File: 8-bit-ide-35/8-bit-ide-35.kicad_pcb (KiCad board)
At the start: 2 copper layers, 214 x 100.3 mm, 21 parts, among them U4 RPI_PICO

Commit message: Small schematic changes. Add outline of XTA board.
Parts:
- moved C1 84.4 mm to (75.1, 32.3)
- moved D1 84.4 mm to (46.7, 32.3)
- moved D2 84.4 mm to (52.4, 32.3)
- moved R10 84.4 mm to (69.0, 35.6)
- moved R11 84.4 mm to (69.0, 38.9)
- moved R12 84.4 mm to (46.6, 42.2)
- moved R14 84.4 mm to (57.8, 42.2)
- moved R2 84.4 mm to (57.8, 38.9)
- moved R4 84.4 mm to (46.6, 38.9)
- moved R7 84.4 mm to (57.8, 35.6)
- moved R9 84.4 mm to (46.6, 35.6)
- moved C3 84.4 mm to (63.8, 32.3)
- moved C4 84.4 mm to (69.4, 32.3)
- moved R1 84.4 mm to (63.4, 38.9)
- moved R3 84.4 mm to (52.2, 38.9)
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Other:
- board size 214 x 100.3 mm -> 222.1 x 98.7 mm

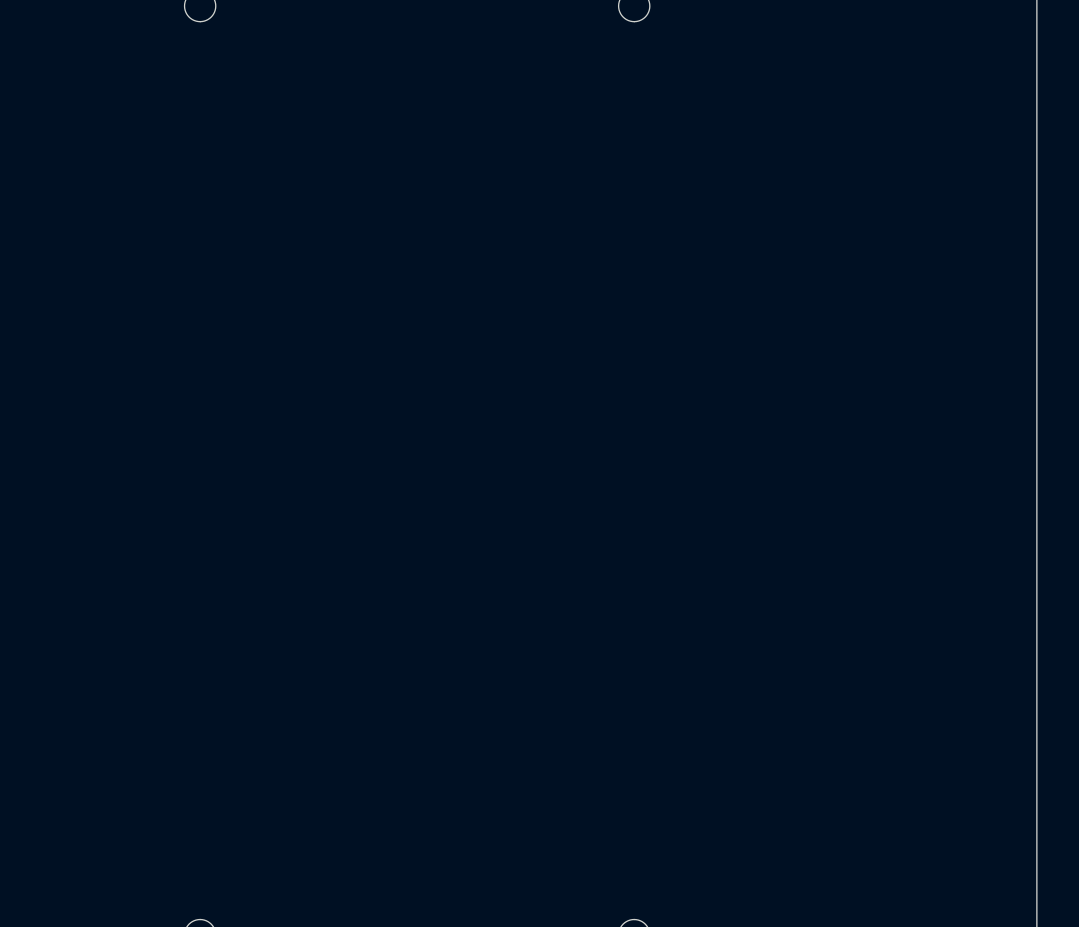
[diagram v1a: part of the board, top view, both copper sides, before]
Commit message: Add power and IDE cable connector. Add holes for mounting to 2.5" to 3.5" HDD adapter.
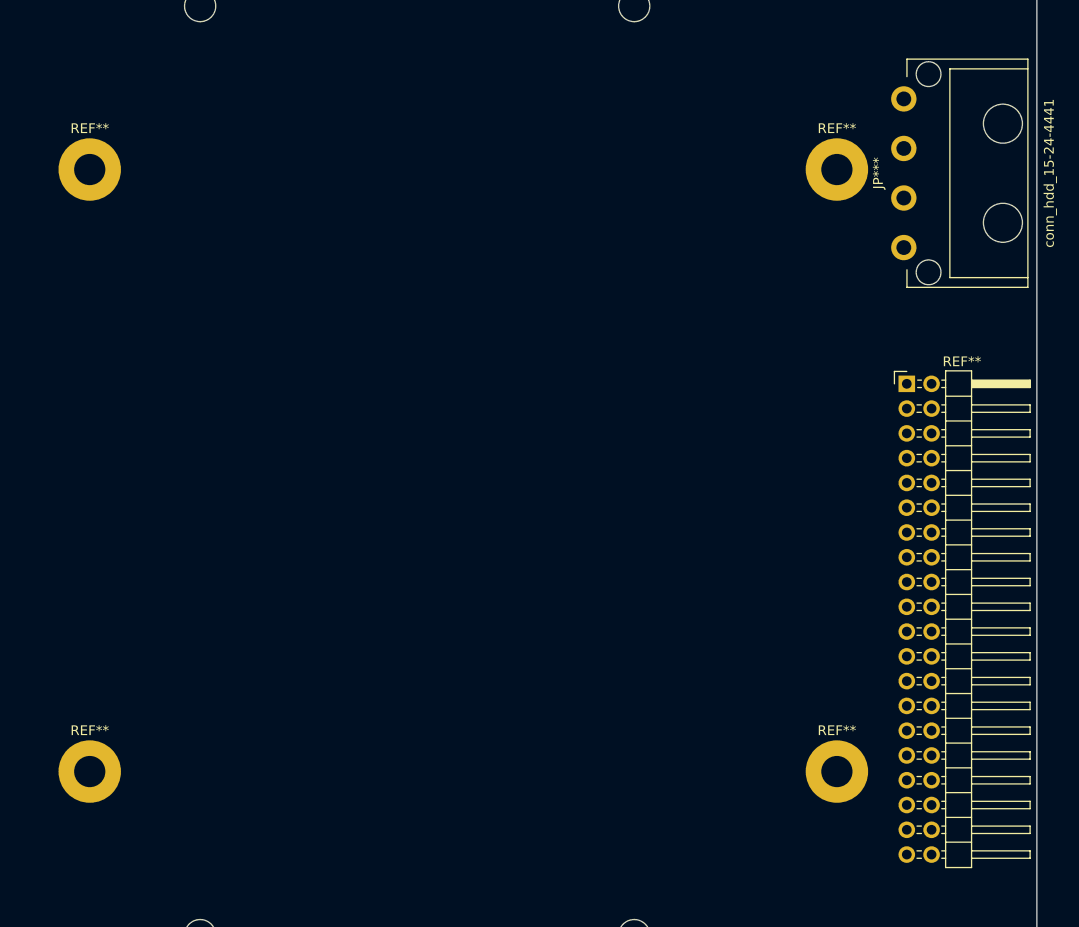
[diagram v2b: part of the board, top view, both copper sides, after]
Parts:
- added REF**: MountingHole_3.2mm_M3_Pad, MountingHole:MountingHole_3.2mm_M3_Pad, F.Cu at (153.1, 49.1)
- added REF**: MountingHole_3.2mm_M3_Pad, MountingHole:MountingHole_3.2mm_M3_Pad, F.Cu at (153.1, 110.9)
- added REF**: MountingHole_3.2mm_M3_Pad, MountingHole:MountingHole_3.2mm_M3_Pad, F.Cu at (229.7, 110.9)
- added REF**: MountingHole_3.2mm_M3_Pad, MountingHole:MountingHole_3.2mm_M3_Pad, F.Cu at (229.7, 49.1)
- added REF**: PinHeader_2x20_P2.54mm_Horizontal, Connector_PinHeader_2.54mm:PinHeader_2x20_P2.54mm_Horizontal, F.Cu at (236.9, 71.1)
- added conn_hdd_15-24-4441: JP***, w_conn_pc:conn_hdd_15-24-4441, F.Cu at (242.6, 49.5)
